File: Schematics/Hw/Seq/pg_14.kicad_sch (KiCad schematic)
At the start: 11 parts, among them U1501 F02, U1502 F153, U1503 F00, U1504 F02, U1505 F02, U1506 F02, U1507 F04, U1508 F02, U1509 F37, U1510 F37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

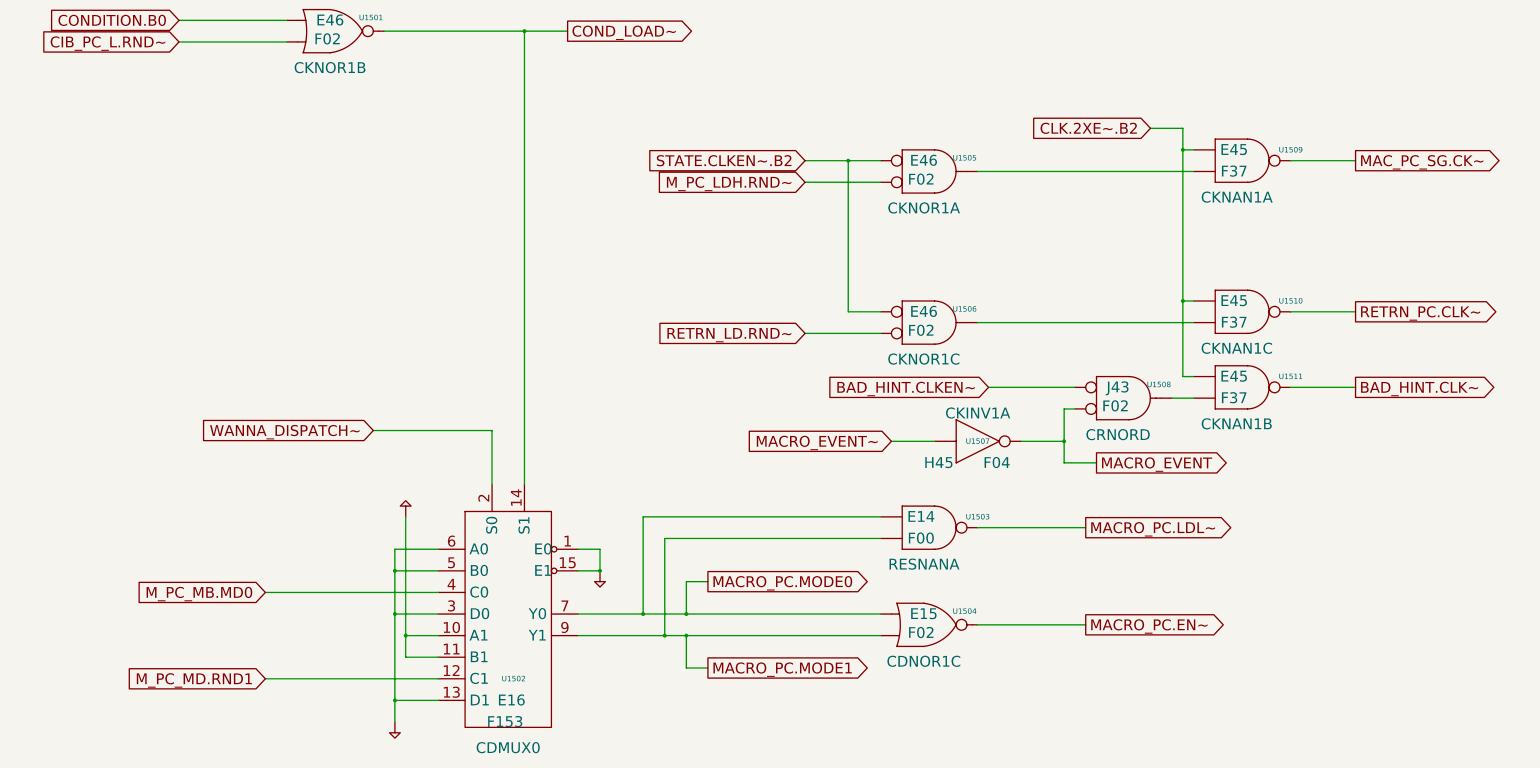
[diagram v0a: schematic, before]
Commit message: Upgrade to KiCad9
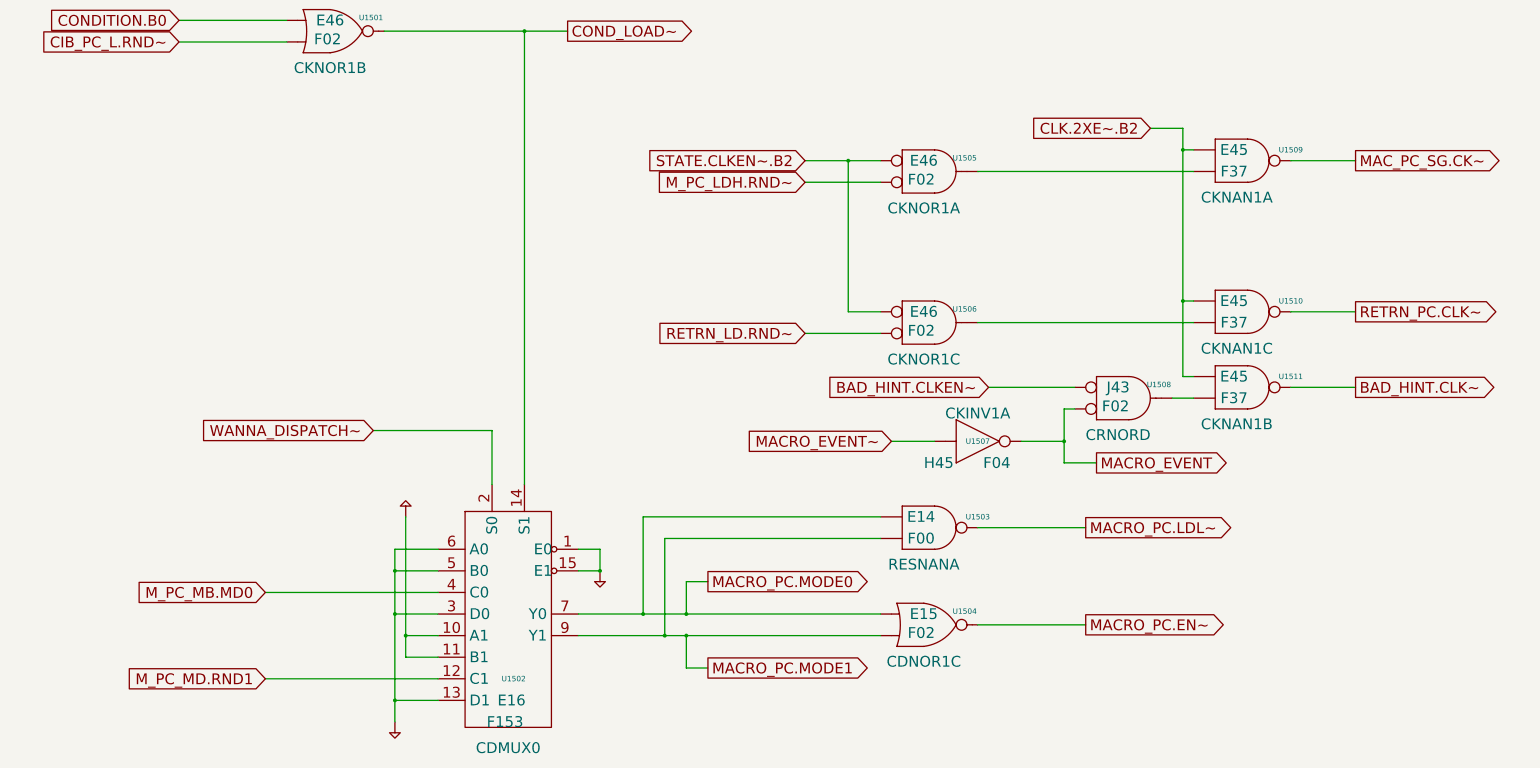
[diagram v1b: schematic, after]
